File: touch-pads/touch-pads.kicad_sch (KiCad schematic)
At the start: 63 parts, among them J1 Conn_01x06_Socket, K1 Conn_01x01, K10 Conn_01x01, K11 Conn_01x01, K12 Conn_01x01, K13 Conn_01x01, K14 Conn_01x01, K15 Conn_01x01, K16 Conn_01x01, K17 Conn_01x01, K18 Conn_01x01, K19 Conn_01x01, K2 Conn_01x01, K20 Conn_01x01, K21 Conn_01x01, K22 Conn_01x01, K23 Conn_01x01, K24 Conn_01x01, K25 Conn_01x01, K26 Conn_01x01, K27 Conn_01x01, K28 Conn_01x01, K29 Conn_01x01, K3 Conn_01x01, K30 Conn_01x01, K31 Conn_01x01, K32 Conn_01x01, K4 Conn_01x01, K5 Conn_01x01, K6 Conn_01x01, K7 Conn_01x01, K8 Conn_01x01, K9 Conn_01x01, U1 CAP1188-1-CP-TR, U2 CAP1188-1-CP-TR, U3 CAP1188-1-CP-TR, U4 CAP1188-1-CP-TR

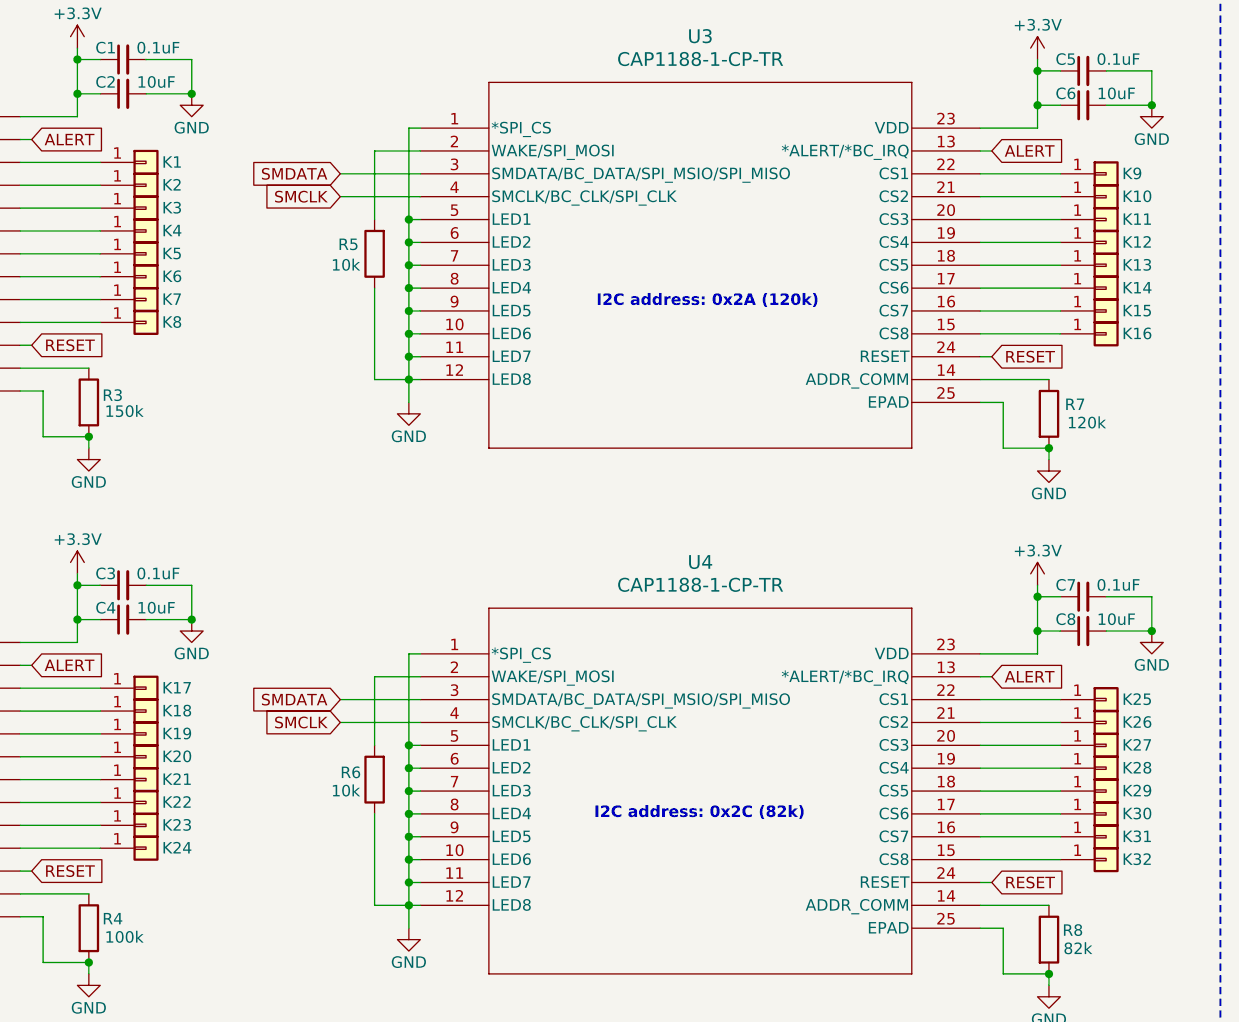
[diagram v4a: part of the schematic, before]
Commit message: update refs and tracks
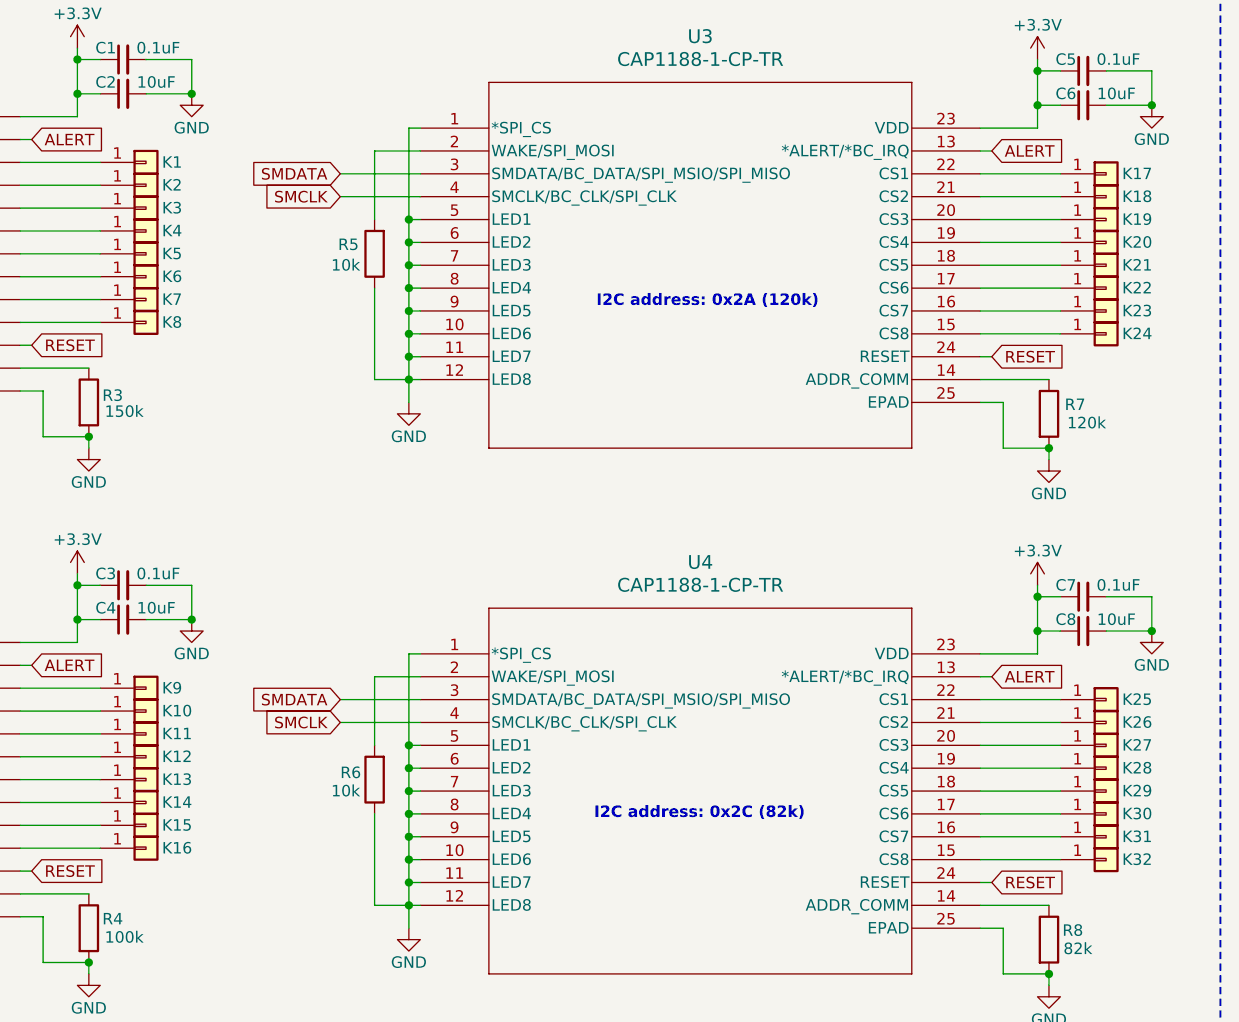
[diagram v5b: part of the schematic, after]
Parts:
- renumbered K18 to K10, K19 to K11, K20 to K12, K21 to K13, K22 to K14, K23 to K15, K24 to K16, K9 to K17, K10 to K18, K11 to K19, K12 to K20, K13 to K21, K14 to K22, K15 to K23, K16 to K24, K17 to K9
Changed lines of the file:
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@@
 		(on_board yes)
 		(dnp no)
-		(property "Reference" "K19"
+		(property "Reference" "K11"
 			(at 116.078 102.87 0)
 			(effects
@@
 			(project "touch-pads"
 				(path "/208e6366-7d11-4576-9309-e3e3af46f0ad"
-					(reference "K19")
+					(reference "K11")
 					(unit 1)
 				)
@@
 		(on_board yes)
 		(dnp no)
-		(property "Reference" "K12"
+		(property "Reference" "K20"
 			(at 222.758 48.26 0)
 			(effects
@@
 			(project "touch-pads"
 				(path "/208e6366-7d11-4576-9309-e3e3af46f0ad"
-					(reference "K12")
+					(reference "K20")
 					(unit 1)
 				)
@@
 		(on_board yes)
 		(dnp no)
-		(property "Reference" "#PWR08"
+		(property "Reference" "#PWR011"
 			(at 143.51 72.39 0)
 			(effects
@@
 			(project "touch-pads"
 				(path "/208e6366-7d11-4576-9309-e3e3af46f0ad"
-					(reference "#PWR08")
+					(reference "#PWR011")
 					(unit 1)
 				)
@@
 		(on_board yes)
 		(dnp no)
-		(property "Reference" "#PWR01"
+		(property "Reference" "#PWR05"
 			(at 106.68 30.48 0)
 			(effects
@@
 			(project "touch-pads"
 				(path "/208e6366-7d11-4576-9309-e3e3af46f0ad"
-					(reference "#PWR01")
+					(reference "#PWR05")
 					(unit 1)
 				)
@@
 		(on_board yes)
 		(dnp no)
-		(property "Reference" "#FLG03"
+		(property "Reference" "#FLG01"
 			(at 31.75 161.925 0)
 			(effects
@@
 			(project "touch-pads"
 				(path "/208e6366-7d11-4576-9309-e3e3af46f0ad"
-					(reference "#FLG03")
+					(reference "#FLG01")
 					(unit 1)
 				)
@@
 		(on_board yes)
 		(dnp no)
-		(property "Reference" "#PWR010"
+		(property "Reference" "#PWR015"
 			(at 214.63 78.74 0)
 			(effects
@@
 			(project "touch-pads"
 				(path "/208e6366-7d11-4576-9309-e3e3af46f0ad"
-					(reference "#PWR010")
+					(reference "#PWR015")
 					(unit 1)
 				)
@@
 		(on_board yes)
 		(dnp no)
-		(property "Reference" "K13"
+		(property "Reference" "K21"
 			(at 222.758 50.8 0)
 			(effects
@@
 			(project "touch-pads"
 				(path "/208e6366-7d11-4576-9309-e3e3af46f0ad"
-					(reference "K13")
+					(reference "K21")
 					(unit 1)
 				)
@@
 		(on_board yes)
 		(dnp no)
-		(property "Reference" "K14"
+		(property "Reference" "K22"
 			(at 222.758 53.34 0)
 			(effects
@@
 			(project "touch-pads"
 				(path "/208e6366-7d11-4576-9309-e3e3af46f0ad"
-					(reference "K14")
+					(reference "K22")
 					(unit 1)
 				)
@@
 		(on_board yes)
 		(dnp no)
-		(property "Reference" "#PWR02"
+		(property "Reference" "#PWR06"
 			(at 106.68 88.9 0)
 			(effects
@@
 			(project "touch-pads"
 				(path "/208e6366-7d11-4576-9309-e3e3af46f0ad"
-					(reference "#PWR02")
+					(reference "#PWR06")
 					(unit 1)
 				)
@@
 		(on_board yes)
 		(dnp no)
-		(property "Reference" "#FLG04"
+		(property "Reference" "#FLG02"
 			(at 31.75 168.275 0)
 			(effects
@@
 			(project "touch-pads"
 				(path "/208e6366-7d11-4576-9309-e3e3af46f0ad"
-					(reference "#FLG04")
+					(reference "#FLG02")
 					(unit 1)
 				)
@@
 		(on_board yes)
 		(dnp no)
-		(property "Reference" "#PWR09"
+		(property "Reference" "#PWR013"
 			(at 213.36 31.75 0)
 			(effects
@@
 			(project "touch-pads"
 				(path "/208e6366-7d11-4576-9309-e3e3af46f0ad"
-					(reference "#PWR09")
+					(reference "#PWR013")
 					(unit 1)
 				)
@@
 		(on_board yes)
 		(dnp no)
-		(property "Reference" "#PWR06"
+		(property "Reference" "#PWR04"
 			(at 40.64 175.26 0)
 			(effects
@@
 			(project "touch-pads"
 				(path "/208e6366-7d11-4576-9309-e3e3af46f0ad"
-					(reference "#PWR06")
+					(reference "#PWR04")
 					(unit 1)
 				)
@@
 		(on_board yes)
 		(dnp no)
-		(property "Reference" "K21"
+		(property "Reference" "K13"
 			(at 116.078 107.95 0)
 			(effects
@@
 			(project "touch-pads"
 				(path "/208e6366-7d11-4576-9309-e3e3af46f0ad"
-					(reference "K21")
+					(reference "K13")
 					(unit 1)
 				)
@@
 		(on_board yes)
 		(dnp no)
-		(property "Reference" "#PWR012"
+		(property "Reference" "#PWR017"
 			(at 226.06 39.37 0)
 			(effects
@@
 			(project "touch-pads"
 				(path "/208e6366-7d11-4576-9309-e3e3af46f0ad"
-					(reference "#PWR012")
+					(reference "#PWR017")
 					(unit 1)
 				)
@@
 		(on_board yes)
 		(dnp no)
-		(property "Reference" "#PWR013"
+		(property "Reference" "#PWR08"
 			(at 107.95 135.89 0)
 			(effects
@@
 			(project "touch-pads"
 				(path "/208e6366-7d11-4576-9309-e3e3af46f0ad"
-					(reference "#PWR013")
+					(reference "#PWR08")
 					(unit 1)
 				)
@@
 		(on_board yes)
 		(dnp no)
-		(property "Reference" "#PWR03"
+		(property "Reference" "#PWR010"
 			(at 119.38 96.52 0)
 			(effects
@@
 			(project "touch-pads"
 				(path "/208e6366-7d11-4576-9309-e3e3af46f0ad"
-					(reference "#PWR03")
+					(reference "#PWR010")
 					(unit 1)
 				)
@@
 		(on_board yes)
 		(dnp no)
-		(property "Reference" "K9"
+		(property "Reference" "K17"
 			(at 222.758 40.64 0)
 			(effects
@@
 			(project "touch-pads"
 				(path "/208e6366-7d11-4576-9309-e3e3af46f0ad"
-					(reference "K9")
+					(reference "K17")
 					(unit 1)
 				)
@@
 		(on_board yes)
 		(dnp no)
-		(property "Reference" "K23"
+		(property "Reference" "K15"
 			(at 116.078 113.03 0)
 			(effects
@@
 			(project "touch-pads"
 				(path "/208e6366-7d11-4576-9309-e3e3af46f0ad"
-					(reference "K23")
+					(reference "K15")
 					(unit 1)
 				)
@@
 		(on_board yes)
 		(dnp no)
-		(property "Reference" "K10"
+		(property "Reference" "K18"
 			(at 222.758 43.18 0)
 			(effects
@@
 			(project "touch-pads"
 				(path "/208e6366-7d11-4576-9309-e3e3af46f0ad"
-					(reference "K10")
+					(reference "K18")
 					(unit 1)
 				)
@@
 		(on_board yes)
 		(dnp no)
-		(property "Reference" "K16"
+		(property "Reference" "K24"
 			(at 222.758 58.42 0)
 			(effects
@@
 			(project "touch-pads"
 				(path "/208e6366-7d11-4576-9309-e3e3af46f0ad"
-					(reference "K16")
+					(reference "K24")
 					(unit 1)
 				)
@@
 		(on_board yes)
 		(dnp no)
-		(property "Reference" "K15"
+		(property "Reference" "K23"
 			(at 222.758 55.88 0)
 			(effects
@@
 			(project "touch-pads"
 				(path "/208e6366-7d11-4576-9309-e3e3af46f0ad"
-					(reference "K15")
+					(reference "K23")
 					(unit 1)
 				)
@@
 		(on_board yes)
 		(dnp no)
-		(property "Reference" "K17"
+		(property "Reference" "K9"
 			(at 116.078 97.79 0)
 			(effects
@@
 			(project "touch-pads"
 				(path "/208e6366-7d11-4576-9309-e3e3af46f0ad"
-					(reference "K17")
+					(reference "K9")
 					(unit 1)
 				)
@@
 		(on_board yes)
 		(dnp no)
-		(property "Reference" "K22"
+		(property "Reference" "K14"
 			(at 116.078 110.49 0)
 			(effects
@@
 			(project "touch-pads"
 				(path "/208e6366-7d11-4576-9309-e3e3af46f0ad"
-					(reference "K22")
+					(reference "K14")
 					(unit 1)
 				)
@@
 		(on_board yes)
 		(dnp no)
-		(property "Reference" "#PWR011"
+		(property "Reference" "#PWR02"
 			(at 36.83 129.54 0)
 			(effects
@@
 			(project "touch-pads"
 				(path "/208e6366-7d11-4576-9309-e3e3af46f0ad"
-					(reference "#PWR011")
+					(reference "#PWR02")
 					(unit 1)
 				)
@@
 		(on_board yes)
 		(dnp no)
-		(property "Reference" "#PWR05"
+		(property "Reference" "#PWR03"
 			(at 40.64 165.1 0)
 			(effects
@@
 			(project "touch-pads"
 				(path "/208e6366-7d11-4576-9309-e3e3af46f0ad"
-					(reference "#PWR05")
+					(reference "#PWR03")
 					(unit 1)
 				)
@@
 		(on_board yes)
 		(dnp no)
-		(property "Reference" "K18"
+		(property "Reference" "K10"
 			(at 116.078 100.33 0)
 			(effects
@@
 			(project "touch-pads"
 				(path "/208e6366-7d11-4576-9309-e3e3af46f0ad"
-					(reference "K18")
+					(reference "K10")
 					(unit 1)
 				)
@@
 		(on_board yes)
 		(dnp no)
-		(property "Reference" "#PWR030"
+		(property "Reference" "#PWR01"
 			(at 36.83 71.12 0)
 			(effects
@@
 			(project ""
 				(path "/208e6366-7d11-4576-9309-e3e3af46f0ad"
-					(reference "#PWR030")
+					(reference "#PWR01")
 					(unit 1)
 				)
@@
 		(on_board yes)
 		(dnp no)
-		(property "Reference" "#PWR014"
+		(property "Reference" "#PWR012"
 			(at 143.51 130.81 0)
 			(effects
@@
 			(project "touch-pads"
 				(path "/208e6366-7d11-4576-9309-e3e3af46f0ad"
-					(reference "#PWR014")
+					(reference "#PWR012")
 					(unit 1)
 				)
@@
 		(on_board yes)
 		(dnp no)
-		(property "Reference" "K24"
+		(property "Reference" "K16"
 			(at 116.078 115.57 0)
 			(effects
@@
 			(project "touch-pads"
 				(path "/208e6366-7d11-4576-9309-e3e3af46f0ad"
-					(reference "K24")
+					(reference "K16")
 					(unit 1)
 				)
@@
 		(on_board yes)
 		(dnp no)
-		(property "Reference" "#PWR04"
+		(property "Reference" "#PWR09"
 			(at 119.38 38.1 0)
 			(effects
@@
 			(project "touch-pads"
 				(path "/208e6366-7d11-4576-9309-e3e3af46f0ad"
-					(reference "#PWR04")
+					(reference "#PWR09")
 					(unit 1)
 				)
@@
 		(on_board yes)
 		(dnp no)
-		(property "Reference" "K20"
+		(property "Reference" "K12"
 			(at 116.078 105.41 0)
 			(effects
@@
 			(project "touch-pads"
 				(path "/208e6366-7d11-4576-9309-e3e3af46f0ad"
-					(reference "K20")
+					(reference "K12")
 					(unit 1)
 				)
@@
 		(on_board yes)
 		(dnp no)
-		(property "Reference" "#PWR015"
+		(property "Reference" "#PWR014"
 			(at 213.36 90.17 0)
 			(effects
@@
 			(project "touch-pads"
 				(path "/208e6366-7d11-4576-9309-e3e3af46f0ad"
-					(reference "#PWR015")
+					(reference "#PWR014")
 					(unit 1)
 				)
@@
 		(on_board yes)
 		(dnp no)
-		(property "Reference" "K11"
+		(property "Reference" "K19"
 			(at 222.758 45.72 0)
 			(effects
@@
 			(project "touch-pads"
 				(path "/208e6366-7d11-4576-9309-e3e3af46f0ad"
-					(reference "K11")
+					(reference "K19")
 					(unit 1)
 				)
@@
 		(on_board yes)
 		(dnp no)
-		(property "Reference" "#PWR017"
+		(property "Reference" "#PWR018"
 			(at 226.06 97.79 0)
 			(effects
@@
 			(project "touch-pads"
 				(path "/208e6366-7d11-4576-9309-e3e3af46f0ad"
-					(reference "#PWR017")
+					(reference "#PWR018")
 					(unit 1)
 				)
